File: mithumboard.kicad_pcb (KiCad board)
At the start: 2 copper layers, 33 parts, among them J1 MJ-4PP-9, J2 MJ-4PP-9, J3 MJ-4PP-9, J4 MJ-4PP-9, SW1 SW_Push, SW10 SW_Push, SW11 SW_Push, SW12 SW_Push, SW13 SW_Push, SW14 SW_Push, SW15 SW_Push, SW16 SW_DIP_x04, SW17 SW_Push, SW2 SW_Push, SW3 SW_Push, SW4 SW_Push, SW5 SW_Push, SW6 SW_Push, SW7 SW_Push, SW8 SW_Push, SW9 SW_Push, U1 MCP23017_SP

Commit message: 位置調整
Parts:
- moved J2 9.03 mm to (60.0, 119.3)
- moved J4 9.03 mm to (60.0, 43.1)
- moved C1 8.94 mm to (112.7, 117.9)
- moved C2 8.94 mm to (117.7, 119.2)
- moved C3 8.94 mm to (73.3, 121.3)
- moved JP1 8.94 mm to (119.1, 47.2)
- moved R1 8.94 mm to (115.3, 45.4)
- moved RN1 8.94 mm to (99.8, 119.8)
- moved SW1 8.94 mm to (71.1, 55.1)
- moved SW10 8.94 mm to (128.2, 55.1)
- moved SW11 8.94 mm to (128.2, 74.1)
- moved SW12 8.94 mm to (128.2, 93.2)
- moved SW13 8.94 mm to (147.3, 55.1)
- moved SW14 8.94 mm to (147.3, 74.1)
- moved SW15 8.94 mm to (147.3, 93.2)
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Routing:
- net INT: track 89.9 -> 91.9 mm
- net SDA: track 97.0 -> 99.1 mm
- net SCL: track 89.5 -> 91.5 mm
- net R1C5: track 71.2 -> 72.6 mm
- net VCC: track 170.7 -> 171.9 mm

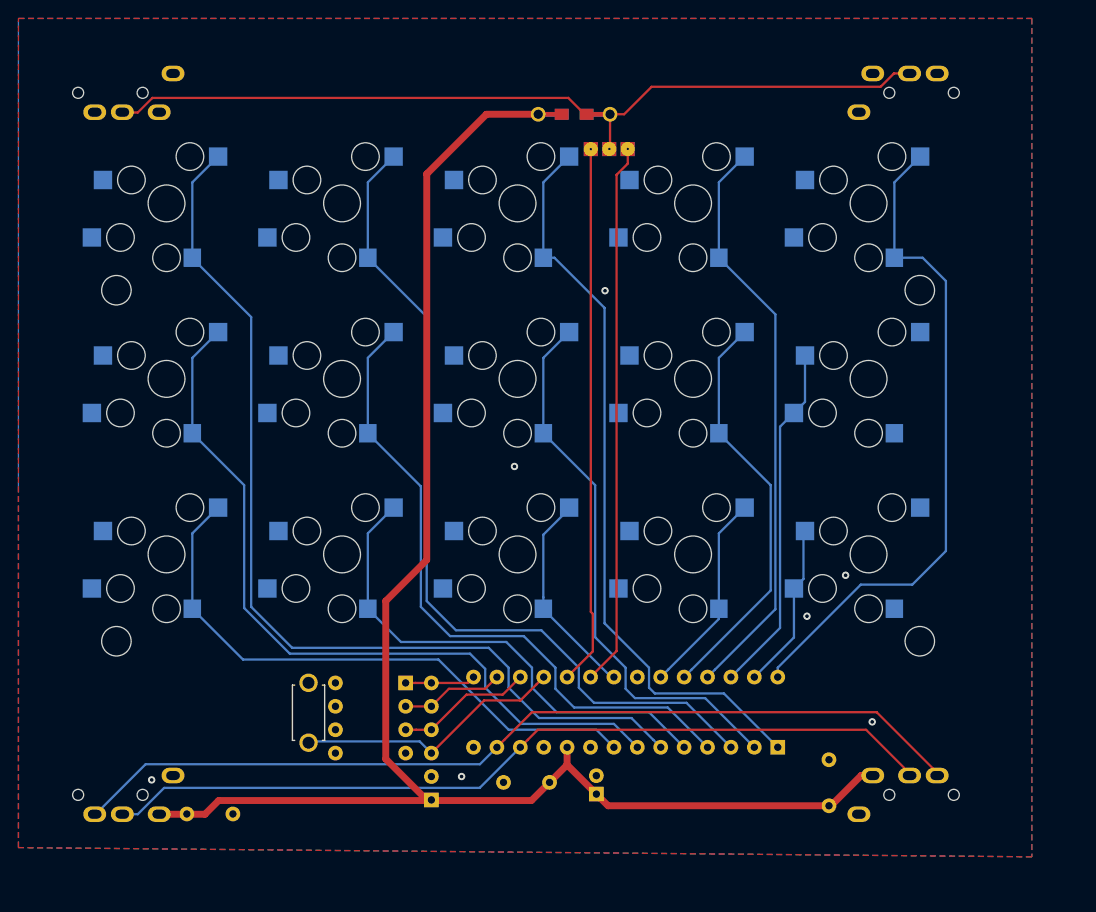
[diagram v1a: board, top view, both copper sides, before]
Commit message: 外枠切った
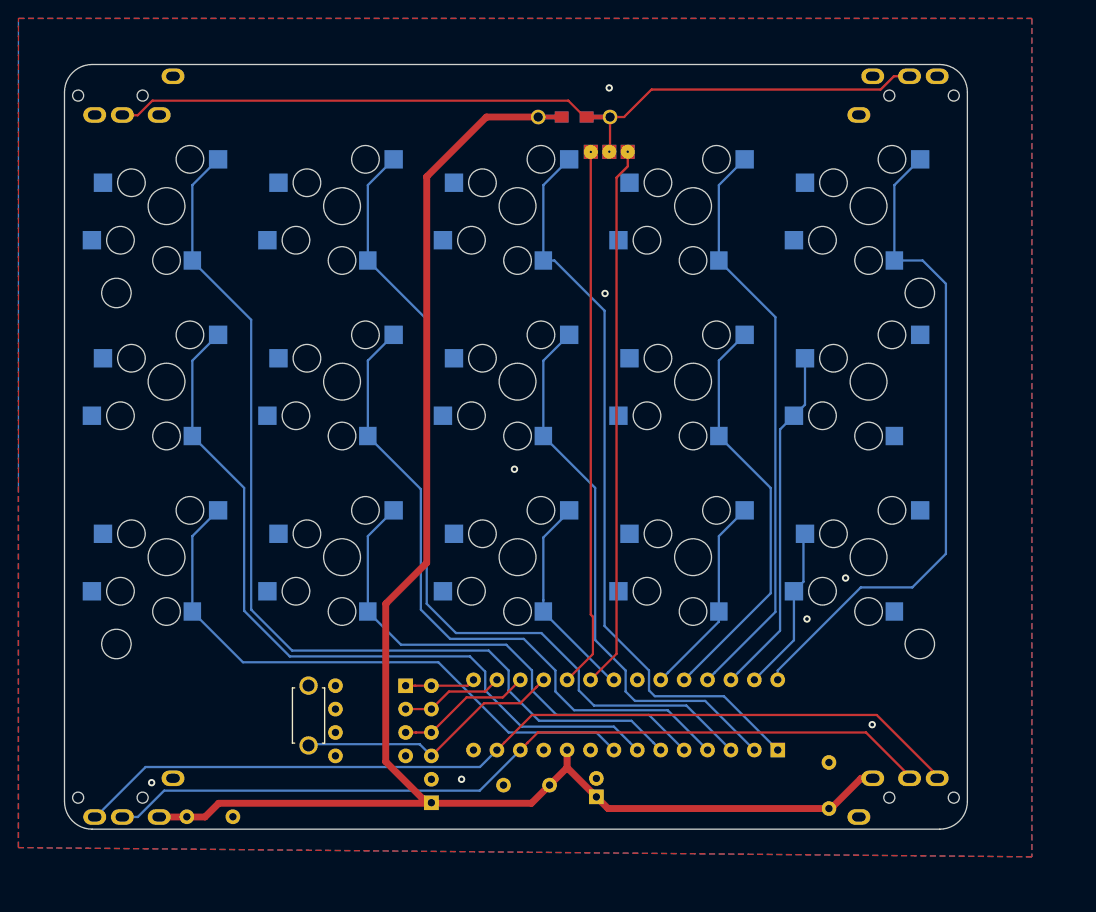
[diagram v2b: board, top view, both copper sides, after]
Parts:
- moved C4 0.30 mm to (143.0, 120.8)
- moved H2 0.30 mm to (65.6, 102.9)
- moved H4 0.30 mm to (152.8, 102.9)
- moved R3C1 0.30 mm to (71.1, 93.5)
- moved R3C2 0.30 mm to (90.1, 93.5)
- moved R3C3 0.30 mm to (109.2, 93.5)
- moved R3C4 0.30 mm to (128.2, 93.5)
- moved R3C5 0.30 mm to (147.3, 93.5)
- moved JP1 0.30 mm to (119.1, 47.5)
- moved R1 0.30 mm to (115.3, 45.7)
- moved C1 0.30 mm to (112.7, 118.2)
- moved C2 0.30 mm to (117.7, 119.5)
- moved C3 0.30 mm to (73.3, 121.6)
- moved H1 0.30 mm to (65.6, 64.8)
- moved H3 0.30 mm to (152.8, 64.8)
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- renumbered SW1 to R1C1, SW4 to R1C2, SW7 to R1C3, SW10 to R1C4, SW13 to R1C5, SW2 to R2C1, SW5 to R2C2, SW8 to R2C3, SW11 to R2C4, SW14 to R2C5, SW3 to R3C1, SW6 to R3C2, SW9 to R3C3, SW12 to R3C4, SW15 to R3C5
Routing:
- net GND: vias 7 -> 8
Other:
- board outline added: 98 x 83 mm

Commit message: TCA9555PWR に置き換え、キースイッチ以外の配線をやり直し
キースイッチへの再配線が残。
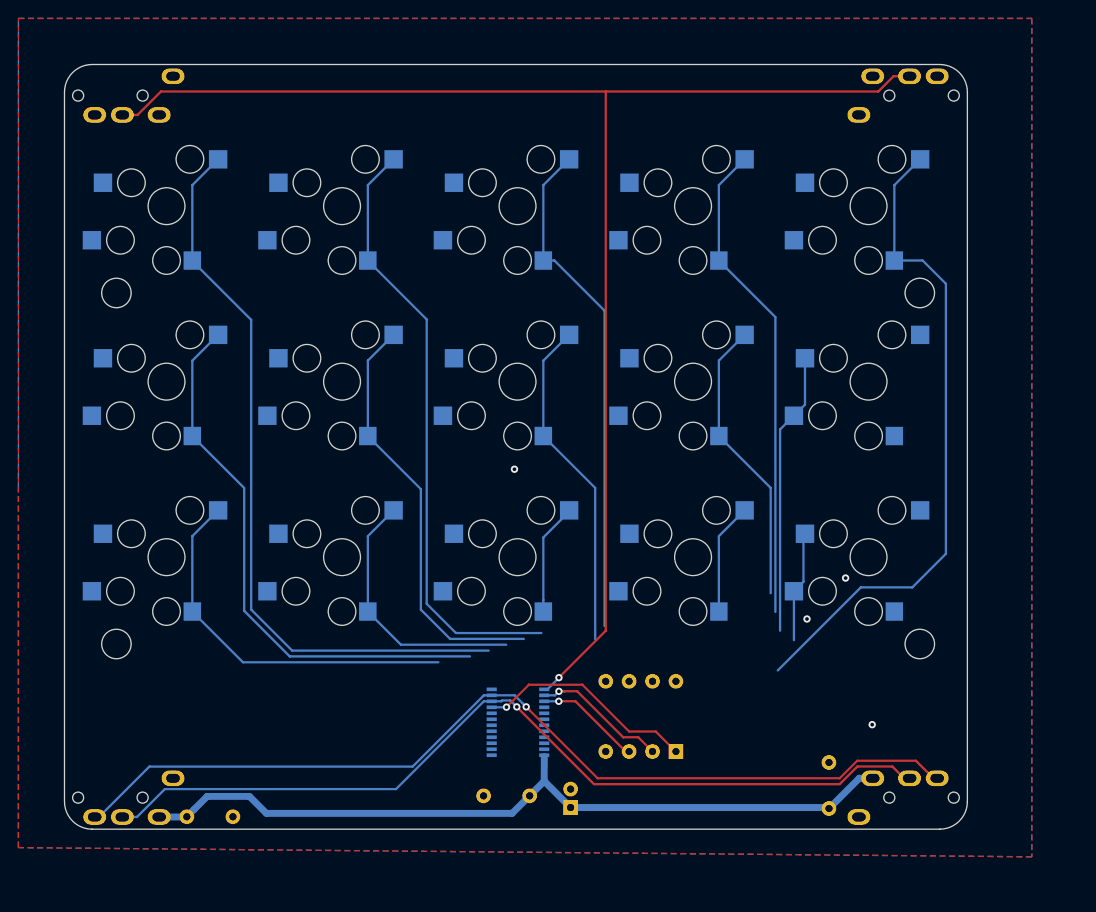
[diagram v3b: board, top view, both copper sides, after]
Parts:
- removed JP1: SolderJumper_3_Bridged12, Keebio-Parts:3_Pin_Jumper
- removed R1: R, Keebio-Parts:Resistor-Hybrid
- removed RN1: 10k, Resistor_THT:R_Array_SIP6
- removed SW17: SW_Push, kbd:ResetSW
- U1: value MCP23017_SP -> TCA9555PWR; footprint Package_DIP:DIP-28_W7.62mm -> Package_SO:TSSOP-24_4.4x7.8mm_P0.65mm
- moved SW16 30.2 mm to (126.4, 114.6), turned to 90 degrees
- moved U1 28.4 mm to (109.2, 111.4), turned to 180 degrees
- moved C2 3.03 mm to (114.9, 120.7)
- moved C1 2.45 mm to (110.5, 119.4)
- renumbered R1C1 to SW1, R1C4 to SW10, R2C4 to SW11, R3C4 to SW12, R1C5 to SW13, R2C5 to SW14, R3C5 to SW15, R2C1 to SW2, R3C1 to SW3, R1C2 to SW4, R2C2 to SW5, R3C2 to SW6, R1C3 to SW7, R2C3 to SW8, R3C3 to SW9
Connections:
- U1 pad 1: R1C3 -> INT
- U1 pad 10: VCC -> R2C1
- U1 pad 11: Net-(U1-Pad11) -> R3C1
- U1 pad 12: SCL -> VCC
- U1 pad 13: SDA -> R3C3
- U1 pad 15: A0 -> R3C4
- U1 pad 16: A1 -> R2C4
- U1 pad 17: A2 -> R1C4
- U1 pad 18: RESET -> R2C5
- U1 pad 19: INTB -> R3C5
- U1 pad 2: R2C3 -> A1
- U1 pad 20: INTA -> R1C5
- U1 pad 21: R3C3 -> A0
- U1 pad 22: Net-(U1-Pad22) -> SCL
- U1 pad 23: R3C4 -> SDA
- U1 pad 24: R2C4 -> GND
- U1 pad 3: R1C2 -> A2
- U1 pad 4: R2C2 -> R1C3
- U1 pad 5: R3C2 -> R2C3
- U1 pad 6: R1C1 -> R1C2
- U1 pad 7: R2C1 -> R2C2
- U1 pad 8: R3C1 -> R3C2
- U1 pad 9: GND -> R1C1
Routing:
- net VCC: track 171.9 -> 85.8 mm
- net INT: track 91.9 -> 155.0 mm, vias 0 -> 1
- net INTA: track 59.0 -> 0.00 mm
- net INTB: track 58.5 -> 0.00 mm
- net RESET: track 29.5 -> 0.00 mm
- net R1C2: track 92.9 -> 65.8 mm
- net R2C2: track 72.1 -> 45.9 mm
- net R1C3: track 81.1 -> 55.5 mm
- net R3C2: track 54.0 -> 28.7 mm
- net R1C1: track 104.7 -> 80.3 mm
- net R2C1: track 83.6 -> 60.0 mm
- net R2C3: track 60.2 -> 36.6 mm
- net R3C1: track 64.2 -> 41.2 mm
- net A0: track 7.63 -> 24.0 mm, vias 0 -> 1
- net R2C4: track 44.8 -> 31.5 mm
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
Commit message: 一応配線完了
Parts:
- moved SW16 0.37 mm to (126.4, 114.9)
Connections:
- SW13 pad 1: GND -> R1C5
- SW13 pad 2: R1C5 -> GND
- SW8 pad 1: GND -> R2C3
- SW8 pad 2: R2C3 -> GND
- SW9 pad 1: GND -> R3C3
- SW9 pad 2: R3C3 -> GND
- U1 pad 10: R2C1 -> R3C5
- U1 pad 11: R3C1 -> Net-(U1-Pad11)
- U1 pad 13: R3C3 -> R3C1
- U1 pad 14: Net-(U1-Pad14) -> R2C1
- U1 pad 15: R3C4 -> R1C1
- U1 pad 16: R2C4 -> R3C2
- U1 pad 17: R1C4 -> R2C2
- U1 pad 18: R2C5 -> R1C2
- U1 pad 19: R3C5 -> R2C3
- U1 pad 20: R1C5 -> R3C3
- U1 pad 5: R2C3 -> R3C4
- U1 pad 6: R1C2 -> R2C4
- U1 pad 7: R2C2 -> R1C4
- U1 pad 8: R3C2 -> R1C5
- U1 pad 9: R1C1 -> R2C5
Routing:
- net R2C4: track 31.5 -> 62.5 mm
- net R3C5: track 12.1 -> 42.1 mm
- net R1C4: track 52.8 -> 82.7 mm
- net R2C5: track 30.7 -> 60.6 mm
- net R3C4: track 12.1 -> 38.7 mm
- net R3C3: track 12.6 -> 26.4 mm
- net R1C3: track 55.5 -> 66.2 mm
- net R3C1: track 41.2 -> 51.1 mm
- net R2C3: track 36.6 -> 46.6 mm
- net R2C1: track 60.0 -> 69.5 mm
- net R1C1: track 80.3 -> 87.9 mm
- net R1C5: track 71.6 -> 79.0 mm
- net R2C2: track 45.9 -> 52.6 mm
- net R3C2: track 28.7 -> 34.2 mm
- net R1C2: track 65.8 -> 71.0 mm
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
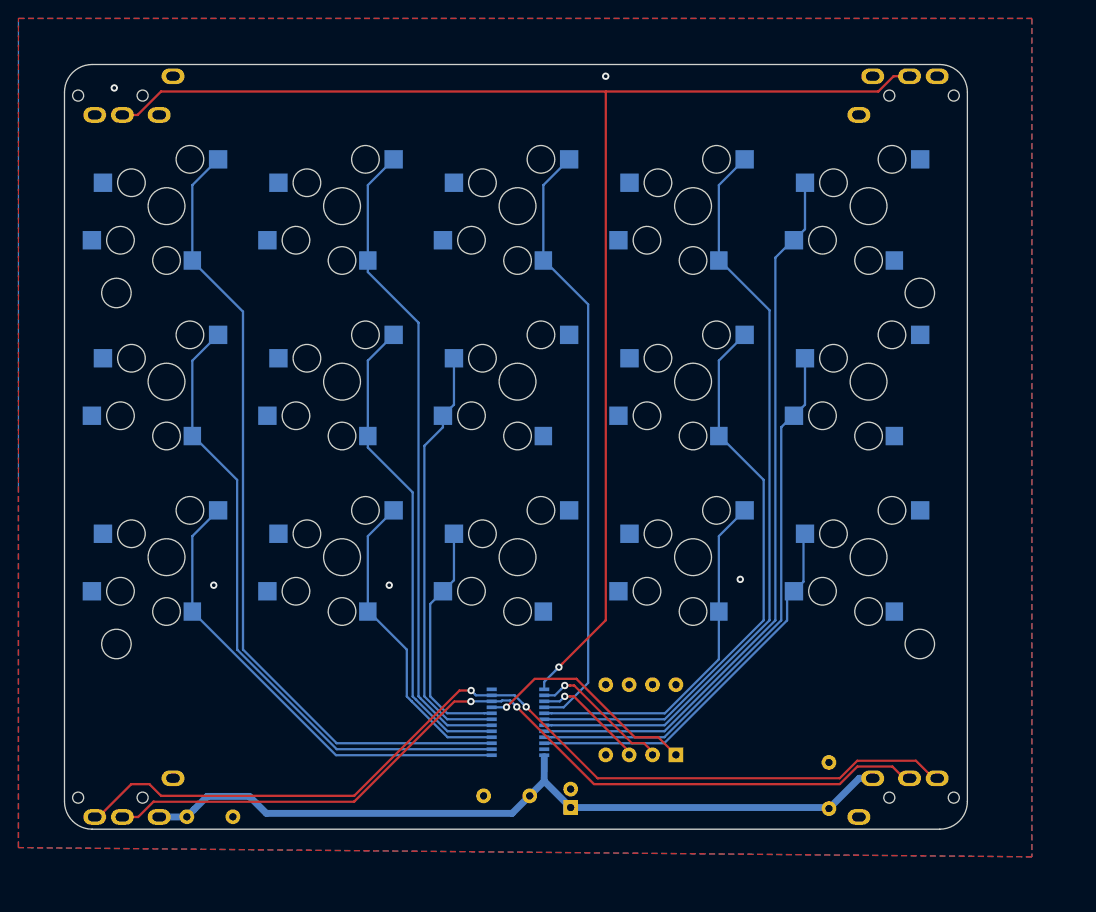
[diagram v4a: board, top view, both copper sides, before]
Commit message: プルアップ抵抗追加・コンデンサと抵抗を表層部品に変更
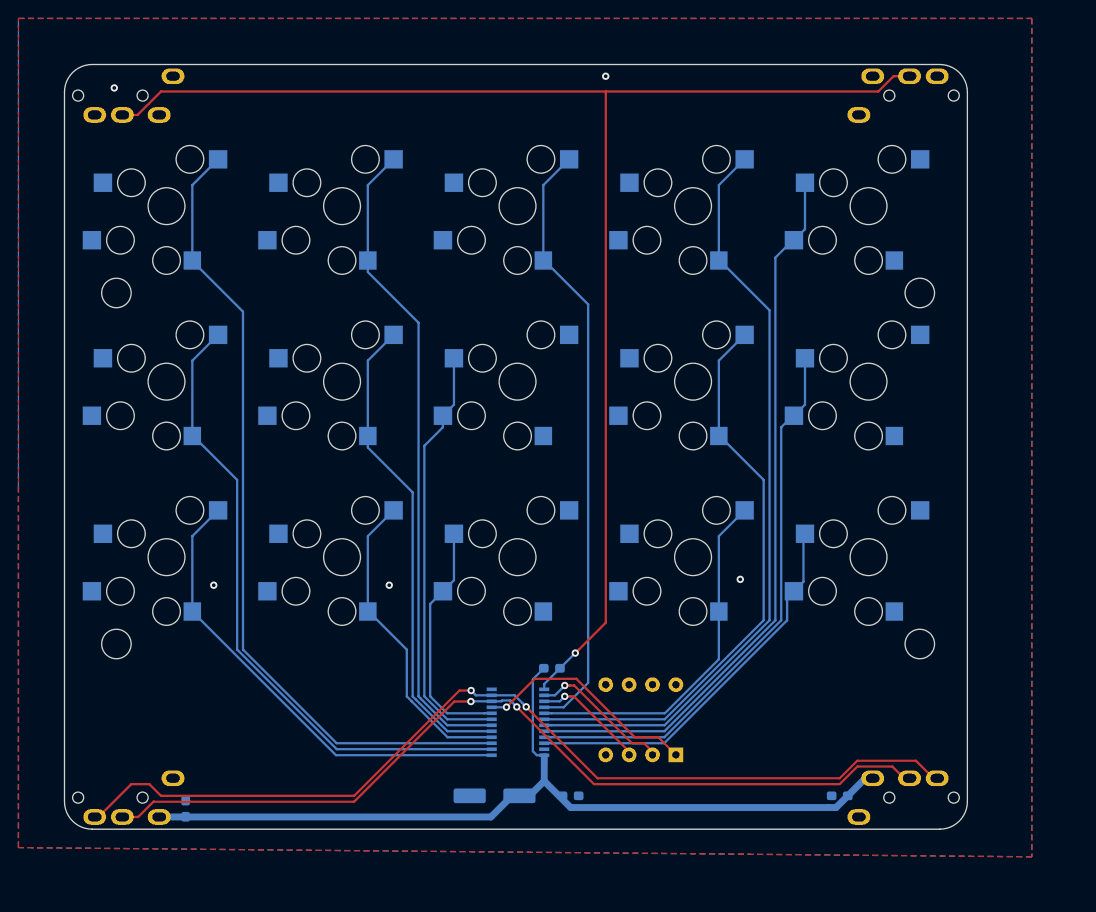
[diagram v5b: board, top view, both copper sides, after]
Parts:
- added R1: 10k, Resistor_SMD:R_0603_1608Metric_Pad1.05x0.95mm_HandSolder, B.Cu at (112.9, 105.5)
- C1, C3, C4: footprint Capacitor_THT:C_Disc_D6.0mm_W2.5mm_P5.00mm -> Capacitor_SMD:C_0603_1608Metric_Pad1.05x0.95mm_HandSolder
- C2: footprint Capacitor_THT:CP_Radial_D5.0mm_P2.00mm -> Capacitor_SMD:CP_Elec_6.3x5.4_Nichicon
- moved C3 70.9 mm to (144.1, 119.4), turned to 180 degrees
- moved C4 69.8 mm to (73.2, 120.8)
- moved C2 8.35 mm to (106.7, 119.4), turned to 180 degrees
- moved C1 4.45 mm to (114.9, 119.4), turned to 0 degrees
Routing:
- net VCC: track 85.8 -> 95.5 mm

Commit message: マウント用スルーホールをM2に変更
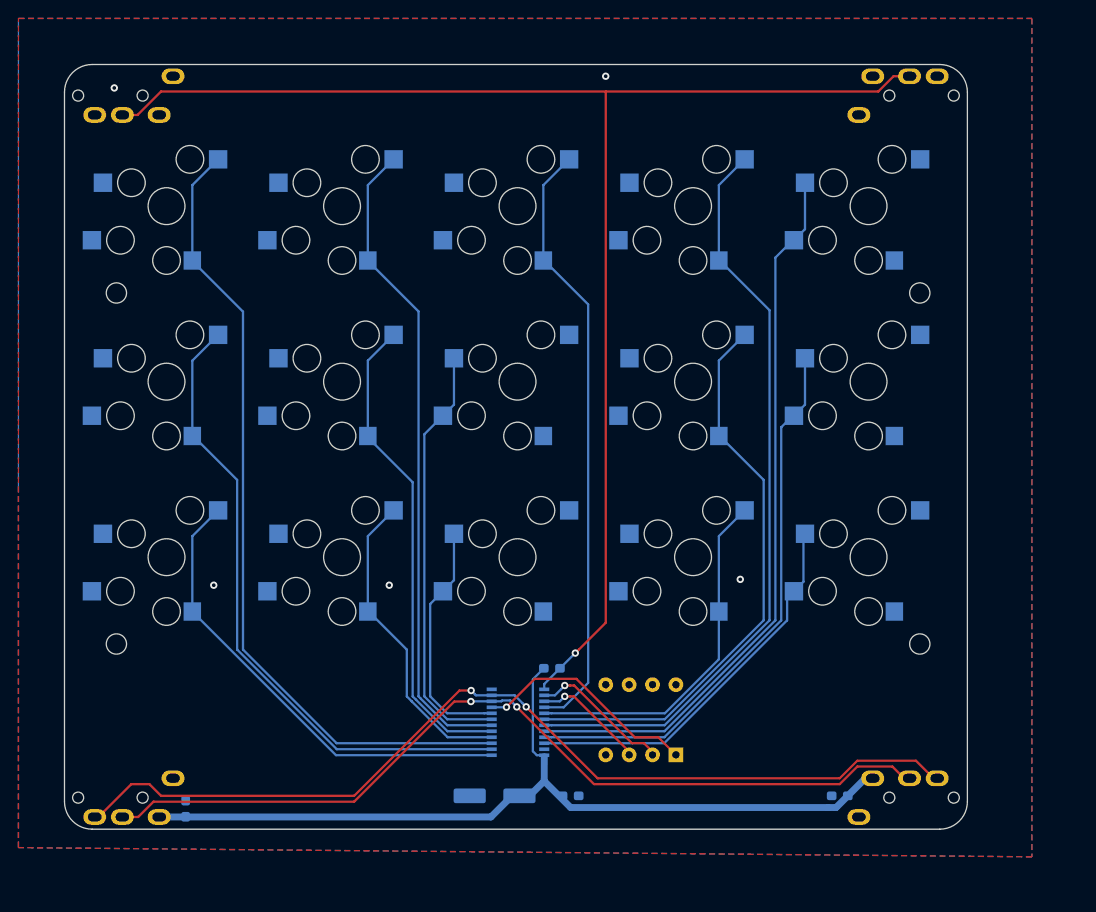
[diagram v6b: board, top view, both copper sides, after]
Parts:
- H1, H2, H3, H4: footprint MountingHole:MountingHole_3.2mm_M3 -> MountingHole:MountingHole_2.2mm_M2
